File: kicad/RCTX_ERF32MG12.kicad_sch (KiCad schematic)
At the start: 101 parts, among them J24 USB, J25 USB, J26 USB_OTG, P1 Nokia 5110 display, P2 BUZZ, P4 LEDs, P5 SD Card, SW2 RESET, U1 MAX2650, U12 MAX2650, U13 EFM32HG310F64G-C-QFN32, U14 USB6B1

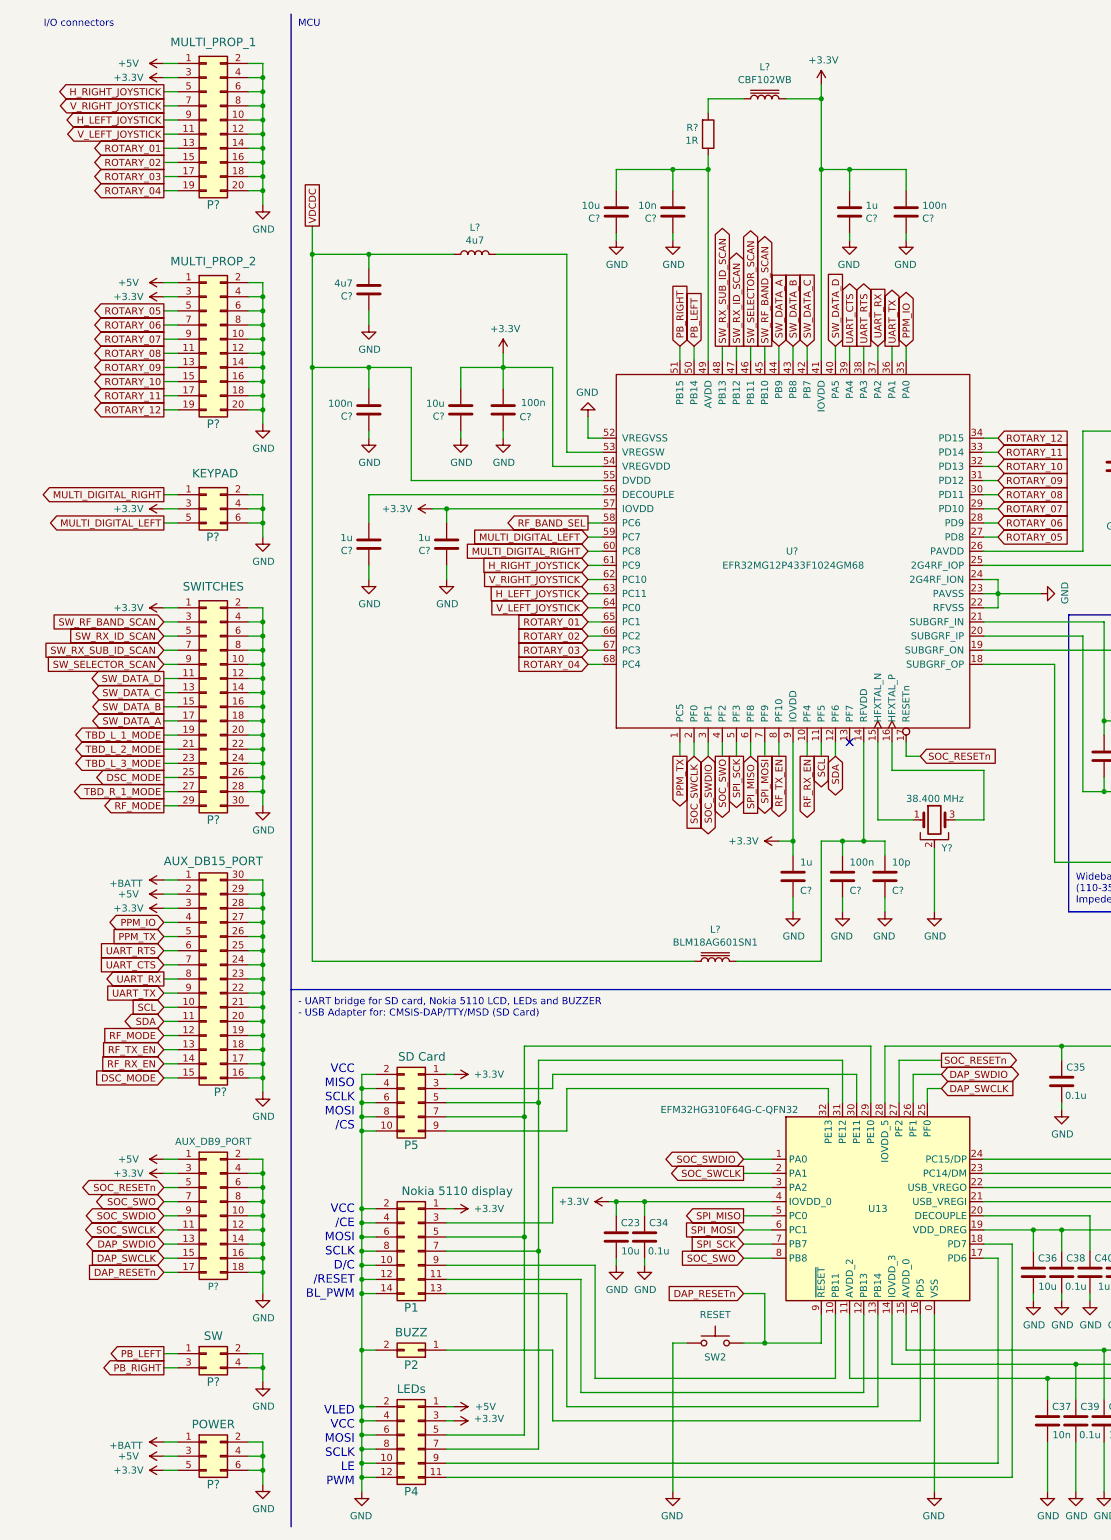
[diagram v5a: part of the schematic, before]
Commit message: Update README.md Updated the Decoder description
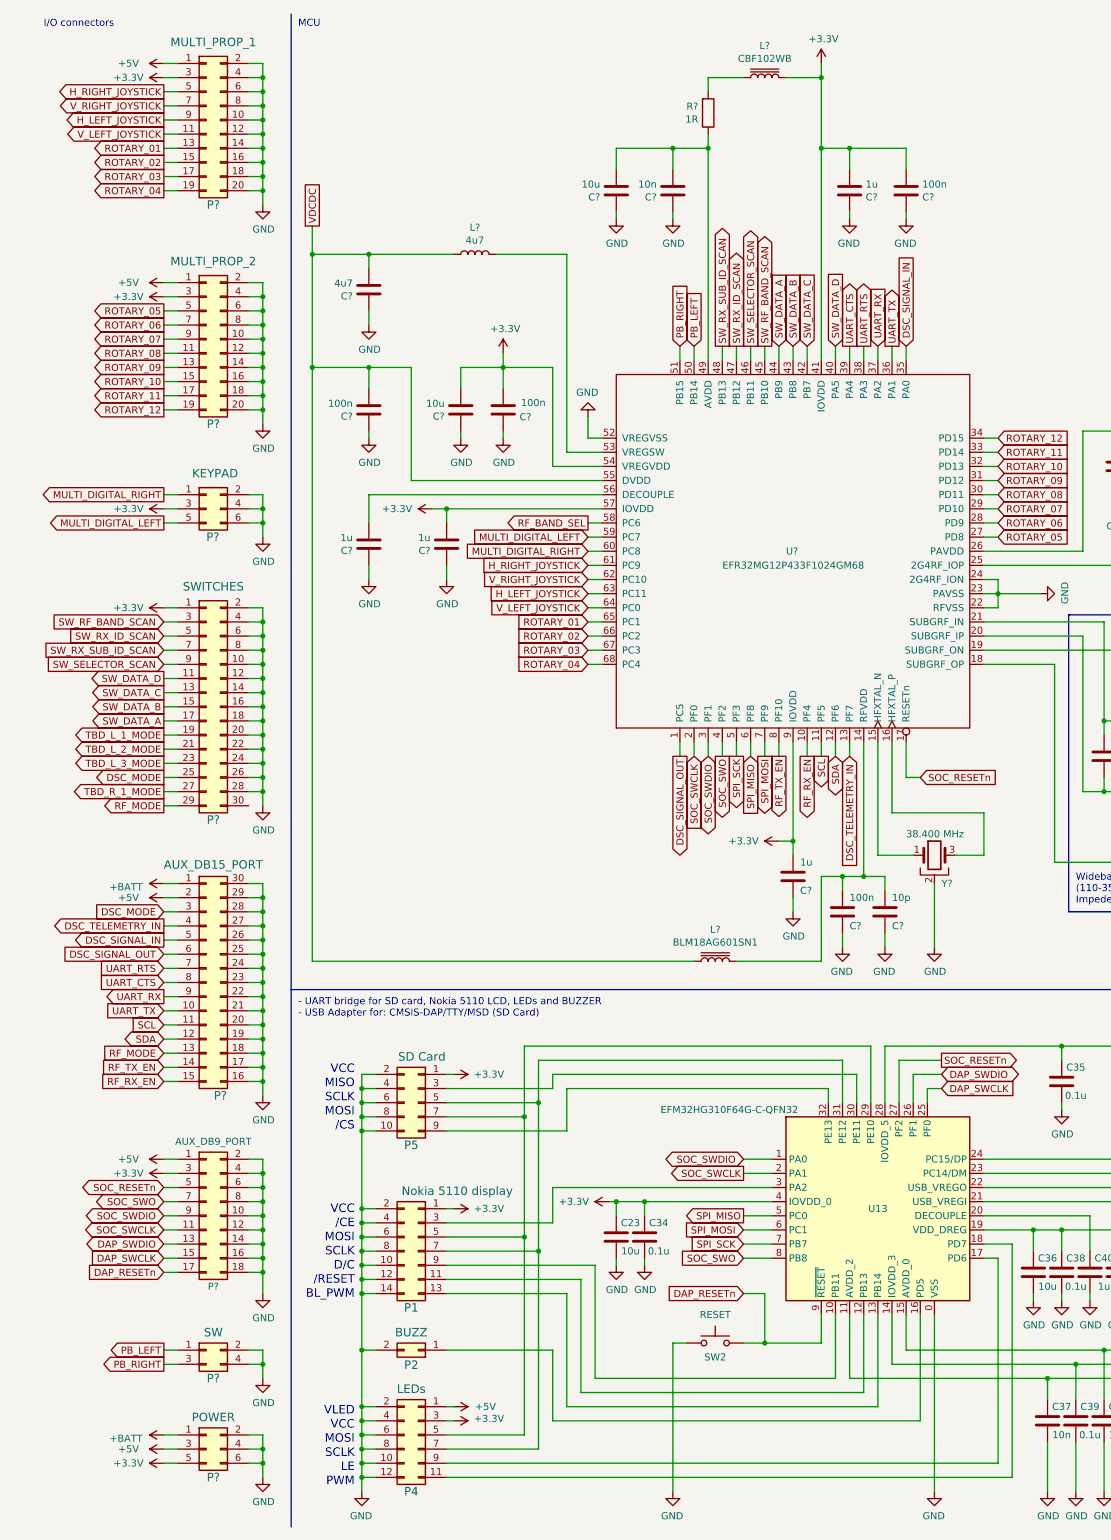
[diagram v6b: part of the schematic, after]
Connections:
- net +3V3: no longer P?.3 (Pin_3)
- net DSC_MODE: now also P?.3 (Pin_3); no longer P?.15 (Pin_15)
- net RF_MODE: now also P?.13 (Pin_13); no longer P?.12 (Pin_12)
- net RF_RX_EN: now also P?.15 (Pin_15); no longer P?.14 (Pin_14)
- net RF_TX_EN: now also P?.14 (Pin_14); no longer P?.13 (Pin_13)
- net SCL: now also P?.11 (Pin_11); no longer P?.10 (Pin_10)
- net SDA: now also P?.12 (Pin_12); no longer P?.11 (Pin_11)
- net UART_CTS: now also P?.8 (Pin_8); no longer P?.7 (Pin_7)
- net UART_RTS: now also P?.7 (Pin_7); no longer P?.6 (Pin_6)
- net UART_RX: now also P?.9 (Pin_9); no longer P?.8 (Pin_8)
- net UART_TX: now also P?.10 (Pin_10); no longer P?.9 (Pin_9)
- net DSC_TELEMETRY_IN: now reaches U?.13 (PF7)
- net DSC_TELEMETRY_IN: now also P?.4 (Pin_4)
- net PPM_IO renamed DSC_SIGNAL_IN
- net DSC_SIGNAL_IN: now also P?.5 (Pin_5); no longer P?.4 (Pin_4)
- net PPM_TX renamed DSC_SIGNAL_OUT
- net DSC_SIGNAL_OUT: now also P?.6 (Pin_6); no longer P?.5 (Pin_5)
- no-connect marks 2 -> 1
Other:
- moved on the sheet: C?, L?, P?, R?, Y?
